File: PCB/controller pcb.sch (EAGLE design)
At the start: 43 parts, among them IC1 MAX481CSA, IC2 MAX481CSA, IC3 STM32F103C8T, U1 TPS62177.DQC, X2 2510-, X4 NC3FAH2, X5 NC3FAH2-0, X7 MINI-USB_4P-85-32004-40X

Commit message: Minor changes to fron PCB. changed positioning of segments and buttons
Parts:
- C1, C2, C3, C4, C5, C6, C7, C8: device rcl:C-EUC0805K -> rcl:C-EUC0603K
- C11: device rcl:C-EUC0805 -> rcl:C-EUC0603K
- R1, R10, R11, R2, R3, R4, R5, R6, R7, R8, R9: device rcl:R-EU_R0805 -> rcl:R-EU_R0603
- X4: value NC3FAH2 -> NC3MBH; device con-neutrik_ag:NC3FAH2 -> con-neutrik_ag:NC3MBH
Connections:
- removed net FP_CS1: IC3MCU.PB0, X2-6.KL
- removed net FP_CS2: IC3MCU.PB1, X2-7.KL
- removed net FP_CS3: IC3MCU.PB2, X2-8.KL
- removed net FP_MISO: IC3MCU.PA6, X2-3.KL
- removed net FP_MOSI: IC3MCU.PA7, X2-4.KL
- removed net FP_SCK: IC3MCU.PA5, X2-5.KL
- new net FP_!RESET: X2-5.KL
- new net FP_SCL: X2-4.KL
- new net FP_SDA: X2-3.KL
- new net FP_SYNC: X2-6.KL
- new net FP_TOUCH1: X2-7.KL
- new net FP_TOUCH2: X2-8.KL
- net +3V3: now also C8.1, IC3MCU.VDDA
- net GND: now also C8.2, IC3MCU.VSSA
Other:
- moved on the sheet: C8

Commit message: pending changes...
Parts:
- added C12: (no value), rcl:C-EUC0603K
- added IC4: MAX481CSA, maxim:MAX481CSA
- added R12, R13, R14: (no value), rcl:R-EU_R0603
- added X1: NC3FAH2-0, con-neutrik_ag:NC3FAH2-0
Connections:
- new net N$11: IC4G$1.B, R12.1, R13.1, X1.3
- new net N$2: IC4G$1.A, R13.2, R14.2, X1.2
- net +3V3: now also C12.1, IC1P.GND, IC4G$1.DE, IC4G$1.RE/, IC4P.GND, R12.2; no longer IC1P.VCC
- net DMX_IN: now also IC4G$1.DI
- net GND: now also C12.2, IC1P.VCC, IC4P.VCC, R14.1, X1.1, X1.G; no longer IC1P.GND
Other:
- note added: "DMX pass through"
- moved on the sheet: IC2, R4, R5, R6, X5

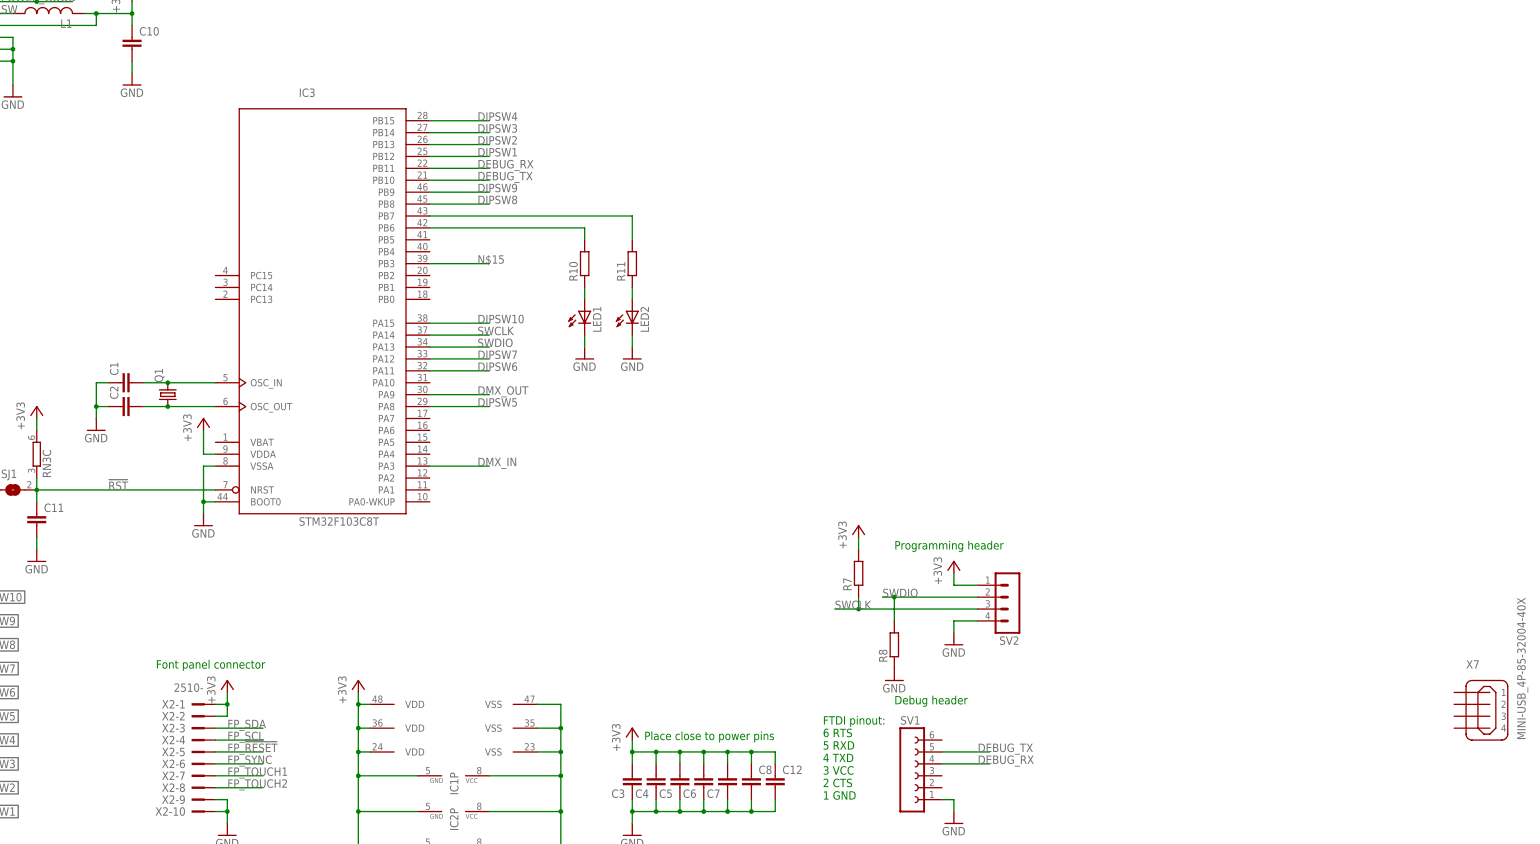
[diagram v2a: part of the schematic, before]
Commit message: Updated to STM32f303
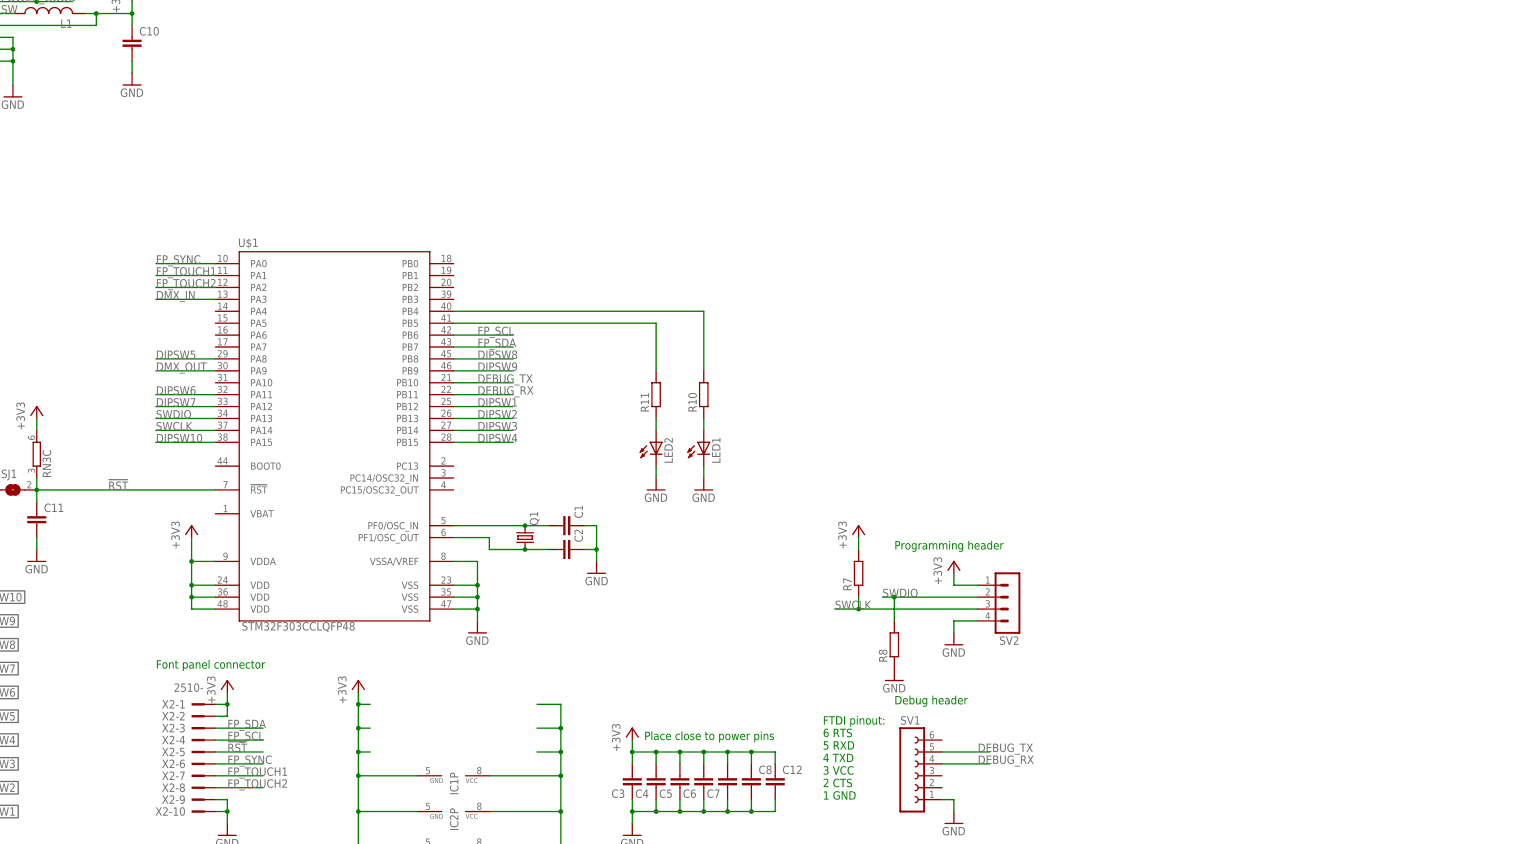
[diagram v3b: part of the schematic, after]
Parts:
- removed IC3: STM32F103C8T, micro-stm:STM32F103C8T
- removed X7: MINI-USB_4P-85-32004-40X, con-cypressindustries:MINI-USB_4P-85-32004-40X
- added U$1: STM32F303CCLQFP48, comp:STM32F303CCLQFP48
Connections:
- removed net FP_!RESET: X2-5.KL
- removed net N$15: IC3MCU.PB3
- net !RST: now also U$1.!RST, X2-5.KL; no longer IC3MCU.NRST
- net +3V3: now also U$1.VDD, U$1.VDD@1, U$1.VDD@2, U$1.VDDA; no longer IC3MCU.VDDA, IC3PWR.VDD@1, IC3PWR.VDD@2, IC3PWR.VDD@3
- net DEBUG_RX: now also U$1.PB11; no longer IC3MCU.PB11
- net DEBUG_TX: now also U$1.PB10; no longer IC3MCU.PB10
- net DIPSW1: now also U$1.PB12; no longer IC3MCU.PB12
- net DIPSW10: now also U$1.PA15; no longer IC3MCU.PA15
- net DIPSW2: now also U$1.PB13; no longer IC3MCU.PB13
- net DIPSW3: now also U$1.PB14; no longer IC3MCU.PB14
- net DIPSW4: now also U$1.PB15; no longer IC3MCU.PB15
- net DIPSW5: now also U$1.PA8; no longer IC3MCU.PA8
- net DIPSW6: now also U$1.PA11; no longer IC3MCU.PA11
- net DIPSW7: now also U$1.PA12; no longer IC3MCU.PA12
- net DIPSW8: now also U$1.PB8; no longer IC3MCU.PB8
- net DIPSW9: now also U$1.PB9; no longer IC3MCU.PB9
- net DMX_IN: now also U$1.PA3; no longer IC3MCU.PA3
- net DMX_OUT: now also U$1.PA9; no longer IC3MCU.PA9
- net FP_SCL: now also U$1.PB6
- net FP_SDA: now also U$1.PB7
- net FP_SYNC: now also U$1.PA0
- net FP_TOUCH1: now also U$1.PA1
- net FP_TOUCH2: now also U$1.PA2
- net GND: now also U$1.VSS, U$1.VSS@1, U$1.VSS@2, U$1.VSSA/VREF; no longer IC3MCU.BOOT0, IC3MCU.VSSA, IC3PWR.VSS@1, IC3PWR.VSS@2, IC3PWR.VSS@3
- net N$12: now also U$1.PB5; no longer IC3MCU.PB7
- net N$13: now also U$1.PB4; no longer IC3MCU.PB6
- net N$4: now also U$1.PF1/OSC_OUT; no longer IC3MCU.OSC_OUT
- net N$5: now also U$1.PF0/OSC_IN; no longer IC3MCU.OSC_IN
- net SWCLK: now also U$1.PA14; no longer IC3MCU.PA14
- net SWDIO: now also U$1.PA13; no longer IC3MCU.PA13
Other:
- moved on the sheet: C1, C2, LED1, LED2, Q1, R10, R11

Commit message: Placed extra decoupling cap and cleaned up some routing
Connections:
- net GND: now also IC1G$1.DI, U$1.BOOT0
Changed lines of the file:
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@@
 <part name="+3V17" library="supply1" library_urn="urn:adsk.eagle:library:371" deviceset="+3V3" device=""/>
 <part name="GND24" library="supply1" library_urn="urn:adsk.eagle:library:371" deviceset="GND" device=""/>
+<part name="GND16" library="supply1" library_urn="urn:adsk.eagle:library:371" deviceset="GND" device=""/>
 </parts>
 <sheets>
@@
 <instance part="GND24" gate="1" x="177.8" y="-12.7" smashed="yes">
 <attribute name="VALUE" x="175.26" y="-15.24" size="1.778" layer="96"/>
+</instance>
+<instance part="GND16" gate="1" x="114.3" y="20.32" smashed="yes">
+<attribute name="VALUE" x="111.76" y="17.78" size="1.778" layer="96"/>
 </instance>
 </instances>
@@
 <wire x1="53.34" y1="81.28" x2="53.34" y2="76.2" width="0.1524" layer="91"/>
 <pinref part="IC1" gate="G$1" pin="DE"/>
-<wire x1="53.34" y1="76.2" x2="53.34" y2="68.58" width="0.1524" layer="91"/>
+<wire x1="53.34" y1="76.2" x2="53.34" y2="71.12" width="0.1524" layer="91"/>
+<wire x1="53.34" y1="71.12" x2="53.34" y2="68.58" width="0.1524" layer="91"/>
 <wire x1="48.26" y1="76.2" x2="53.34" y2="76.2" width="0.1524" layer="91"/>
 <junction x="53.34" y="76.2"/>
+<pinref part="IC1" gate="G$1" pin="DI"/>
+<wire x1="48.26" y1="71.12" x2="53.34" y2="71.12" width="0.1524" layer="91"/>
+<junction x="53.34" y="71.12"/>
 </segment>
 <segment>
@@
 <junction x="177.8" y="-2.54"/>
 </segment>
+<segment>
+<pinref part="U$1" gate="G$1" pin="BOOT0"/>
+<pinref part="GND16" gate="1" pin="GND"/>
+<wire x1="121.92" y1="22.86" x2="114.3" y2="22.86" width="0.1524" layer="91"/>
+</segment>
 </net>

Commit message: Finalized PCBs
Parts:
- removed L1: (no value), rcl:L-USWE-TPC
- added L2: LPS4018, inductor-coilcraft:LPS4018
- C10: value (none) -> 22u
- C9: value (none) -> 2.2uF
- R9: value (none) -> 100K
- renumbered SV2 to PROG, U$1 to IC3, U1 to IC5
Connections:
- net +3V3: now also L2.2; no longer L1.2
- net SW: now also L2.1; no longer L1.1

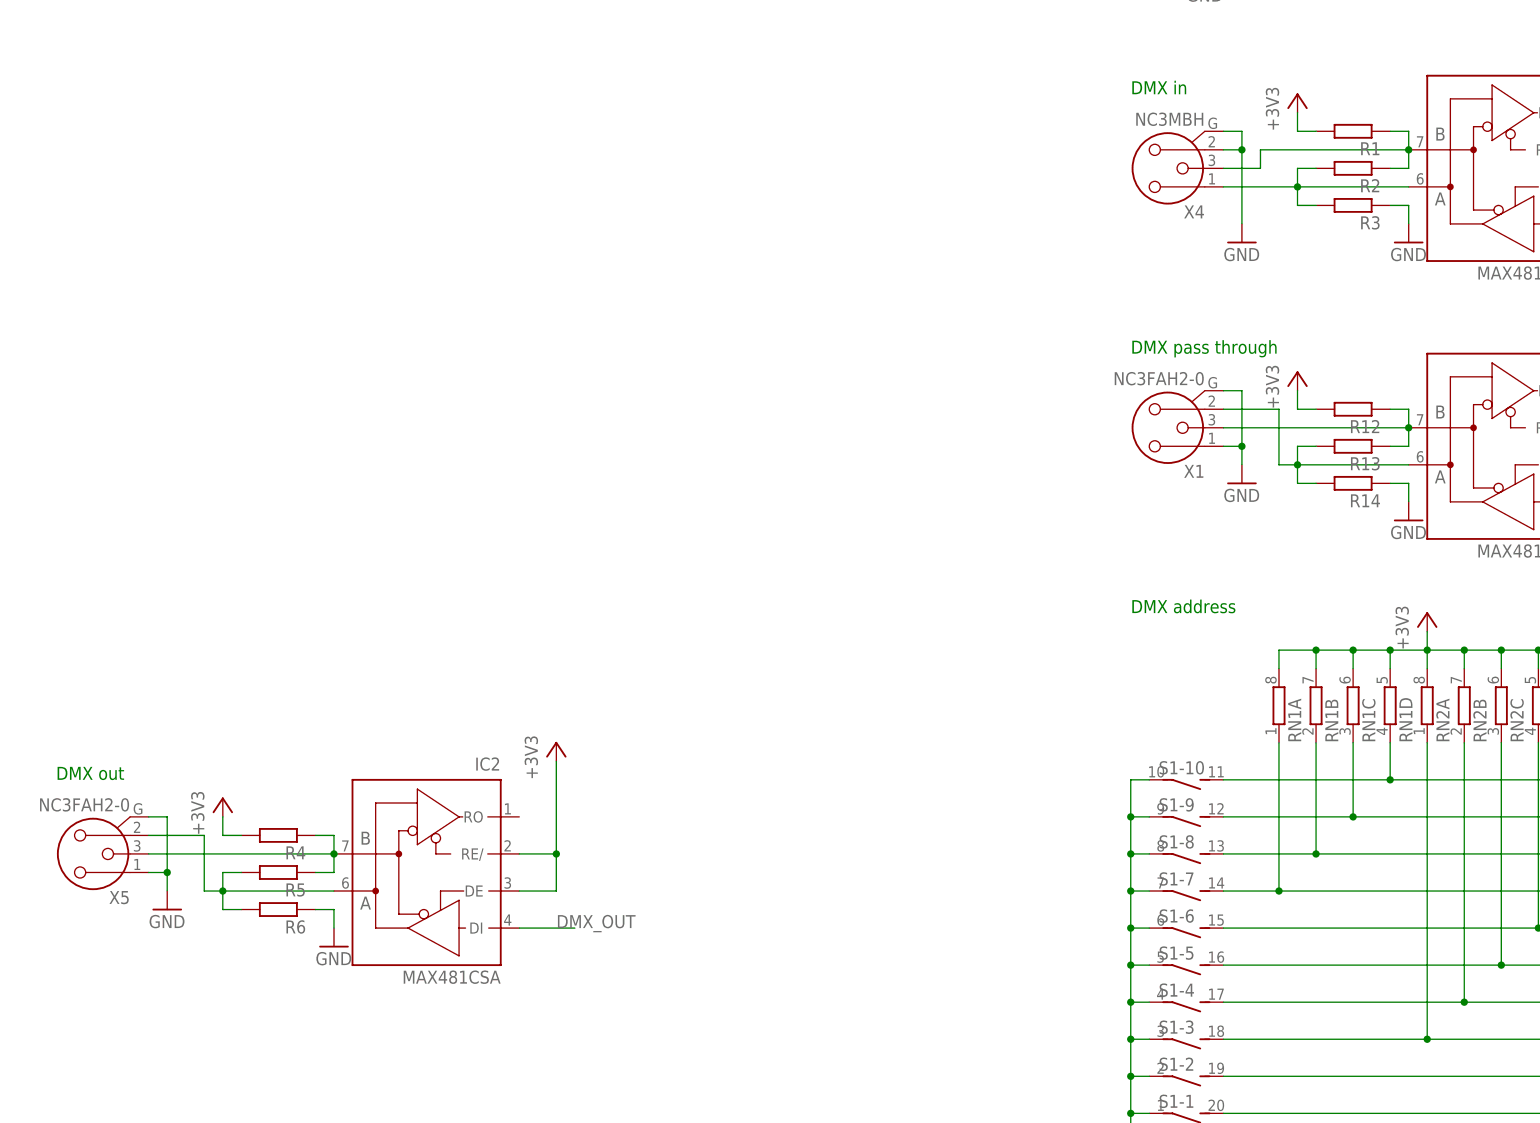
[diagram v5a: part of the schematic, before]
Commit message: fixed pinout on pcb, added test effect
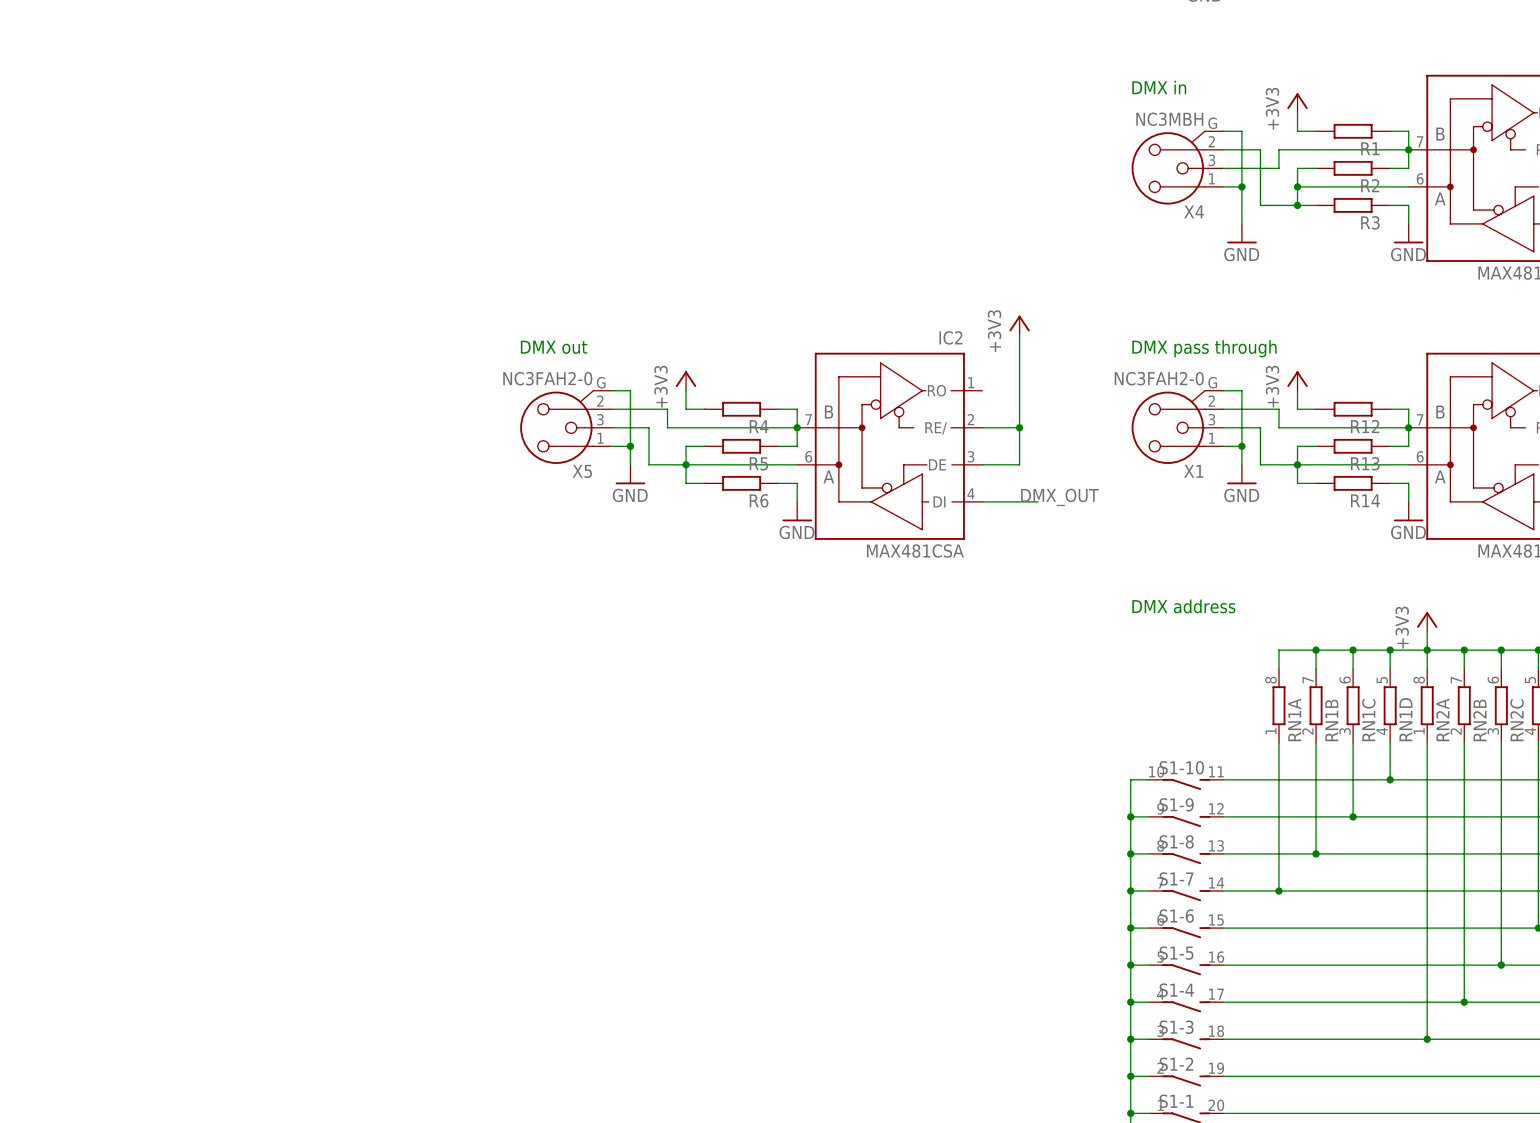
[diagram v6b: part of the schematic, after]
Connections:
- removed net N$11: IC4G$1.B, R12.1, R13.1, X1.3
- removed net N$6: IC1G$1.A, R2.2, R3.2, X4.1
- new net N$15: IC4G$1.B, R12.1, R13.1, X1.2
- new net N$16: IC1G$1.A, R2.2, R3.2, X4.2
- net GND: now also X4.1; no longer X4.2
- net N$2: now also X1.3; no longer X1.2
- net N$7: now also X5.3; no longer X5.2
- net N$8: now also X5.2; no longer X5.3
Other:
- moved on the sheet: IC2, R4, R5, R6, X5
